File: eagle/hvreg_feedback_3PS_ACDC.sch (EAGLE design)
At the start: 17 parts

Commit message: capacitor bank
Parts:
- C5, C6: device rcl:C-US225-108X268 -> rcl:C-US275-205X316
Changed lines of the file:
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@@
 <grid distance="0.1" unitdist="inch" unit="inch" style="lines" multiple="1" display="no" altdistance="0.01" altunitdist="inch" altunit="inch"/>
 <layers>
-<layer number="1" name="Top" color="4" fill="1" visible="no" active="no"/>
-<layer number="2" name="Route2" color="1" fill="3" visible="no" active="no"/>
-<layer number="3" name="Route3" color="4" fill="3" visible="no" active="no"/>
-<layer number="4" name="Route4" color="1" fill="4" visible="no" active="no"/>
-<layer number="5" name="Route5" color="4" fill="4" visible="no" active="no"/>
-<layer number="6" name="Route6" color="1" fill="8" visible="no" active="no"/>
-<layer number="7" name="Route7" color="4" fill="8" visible="no" active="no"/>
-<layer number="8" name="Route8" color="1" fill="2" visible="no" active="no"/>
-<layer number="9" name="Route9" color="4" fill="2" visible="no" active="no"/>
-<layer number="10" name="Route10" color="1" fill="7" visible="no" active="no"/>
-<layer number="11" name="Route11" color="4" fill="7" visible="no" active="no"/>
-<layer number="12" name="Route12" color="1" fill="5" visible="no" active="no"/>
-<layer number="13" name="Route13" color="4" fill="5" visible="no" active="no"/>
-<layer number="14" name="Route14" color="1" fill="6" visible="no" active="no"/>
-<layer number="15" name="Route15" color="4" fill="6" visible="no" active="no"/>
-<layer number="16" name="Bottom" color="1" fill="1" visible="no" active="no"/>
-<layer number="17" name="Pads" color="2" fill="1" visible="no" active="no"/>
-<layer number="18" name="Vias" color="2" fill="1" visible="no" active="no"/>
-<layer number="19" name="Unrouted" color="6" fill="1" visible="no" active="no"/>
-<layer number="20" name="Dimension" color="15" fill="1" visible="no" active="no"/>
-<layer number="21" name="tPlace" color="7" fill="1" visible="no" active="no"/>
-<layer number="22" name="bPlace" color="7" fill="1" visible="no" active="no"/>
-<layer number="23" name="tOrigins" color="15" fill="1" visible="no" active="no"/>
-<layer number="24" name="bOrigins" color="15" fill="1" visible="no" active="no"/>
-<layer number="25" name="tNames" color="7" fill="1" visible="no" active="no"/>
-<layer number="26" name="bNames" color="7" fill="1" visible="no" active="no"/>
-<layer number="27" name="tValues" color="7" fill="1" visible="no" active="no"/>
-<layer number="28" name="bValues" color="7" fill="1" visible="no" active="no"/>
+<layer number="1" name="Top" color="4" fill="1" visible="yes" active="no"/>
+<layer number="2" name="Route2" color="1" fill="3" visible="yes" active="no"/>
+<layer number="3" name="Route3" color="4" fill="3" visible="yes" active="no"/>
+<layer number="4" name="Route4" color="1" fill="4" visible="yes" active="no"/>
+<layer number="5" name="Route5" color="4" fill="4" visible="yes" active="no"/>
+<layer number="6" name="Route6" color="1" fill="8" visible="yes" active="no"/>
+<layer number="7" name="Route7" color="4" fill="8" visible="yes" active="no"/>
+<layer number="8" name="Route8" color="1" fill="2" visible="yes" active="no"/>
+<layer number="9" name="Route9" color="4" fill="2" visible="yes" active="no"/>
+<layer number="10" name="Route10" color="1" fill="7" visible="yes" active="no"/>
+<layer number="11" name="Route11" color="4" fill="7" visible="yes" active="no"/>
+<layer number="12" name="Route12" color="1" fill="5" visible="yes" active="no"/>
+<layer number="13" name="Route13" color="4" fill="5" visible="yes" active="no"/>
+<layer number="14" name="Route14" color="1" fill="6" visible="yes" active="no"/>
+<layer number="15" name="Route15" color="4" fill="6" visible="yes" active="no"/>
+<layer number="16" name="Bottom" color="1" fill="1" visible="yes" active="no"/>
+<layer number="17" name="Pads" color="2" fill="1" visible="yes" active="no"/>
+<layer number="18" name="Vias" color="2" fill="1" visible="yes" active="no"/>
+<layer number="19" name="Unrouted" color="6" fill="1" visible="yes" active="no"/>
+<layer number="20" name="Dimension" color="15" fill="1" visible="yes" active="no"/>
+<layer number="21" name="tPlace" color="7" fill="1" visible="yes" active="no"/>
+<layer number="22" name="bPlace" color="7" fill="1" visible="yes" active="no"/>
+<layer number="23" name="tOrigins" color="15" fill="1" visible="yes" active="no"/>
+<layer number="24" name="bOrigins" color="15" fill="1" visible="yes" active="no"/>
+<layer number="25" name="tNames" color="7" fill="1" visible="yes" active="no"/>
+<layer number="26" name="bNames" color="7" fill="1" visible="yes" active="no"/>
+<layer number="27" name="tValues" color="7" fill="1" visible="yes" active="no"/>
+<layer number="28" name="bValues" color="7" fill="1" visible="yes" active="no"/>
 <layer number="29" name="tStop" color="7" fill="3" visible="no" active="no"/>
 <layer number="30" name="bStop" color="7" fill="6" visible="no" active="no"/>
@@
 <layer number="35" name="tGlue" color="7" fill="4" visible="no" active="no"/>
 <layer number="36" name="bGlue" color="7" fill="5" visible="no" active="no"/>
-<layer number="37" name="tTest" color="7" fill="1" visible="no" active="no"/>
-<layer number="38" name="bTest" color="7" fill="1" visible="no" active="no"/>
+<layer number="37" name="tTest" color="7" fill="1" visible="yes" active="no"/>
+<layer number="38" name="bTest" color="7" fill="1" visible="yes" active="no"/>
 <layer number="39" name="tKeepout" color="4" fill="11" visible="no" active="no"/>
 <layer number="40" name="bKeepout" color="1" fill="11" visible="no" active="no"/>
@@
 <layer number="44" name="Drills" color="7" fill="1" visible="no" active="no"/>
 <layer number="45" name="Holes" color="7" fill="1" visible="no" active="no"/>
-<layer number="46" name="Milling" color="3" fill="1" visible="no" active="no"/>
-<layer number="47" name="Measures" color="7" fill="1" visible="no" active="no"/>
-<layer number="48" name="Document" color="7" fill="1" visible="no" active="no"/>
-<layer number="49" name="Reference" color="7" fill="1" visible="no" active="no"/>
-<layer number="50" name="dxf" color="7" fill="1" visible="no" active="no"/>
-<layer number="51" name="tDocu" color="7" fill="1" visible="no" active="no"/>
-<layer number="52" name="bDocu" color="7" fill="1" visible="no" active="no"/>
-<layer number="53" name="tGND_GNDA" color="7" fill="9" visible="no" active="no"/>
-<layer number="54" name="bGND_GNDA" color="1" fill="9" visible="no" active="no"/>
-<layer number="56" name="wert" color="7" fill="1" visible="no" active="no"/>
+<layer number="46" name="Milling" color="3" fill="1" visible="yes" active="no"/>
+<layer number="47" name="Measures" color="7" fill="1" visible="yes" active="no"/>
+<layer number="48" name="Document" color="7" fill="1" visible="yes" active="no"/>
+<layer number="49" name="Reference" color="7" fill="1" visible="yes" active="no"/>
+<layer number="50" name="dxf" color="7" fill="1" visible="yes" active="no"/>
+<layer number="51" name="tDocu" color="7" fill="1" visible="yes" active="no"/>
+<layer number="52" name="bDocu" color="7" fill="1" visible="yes" active="no"/>
+<layer number="53" name="tGND_GNDA" color="7" fill="9" visible="yes" active="no"/>
+<layer number="54" name="bGND_GNDA" color="1" fill="9" visible="yes" active="no"/>
+<layer number="56" name="wert" color="7" fill="1" visible="yes" active="no"/>
 <layer number="90" name="Modules" color="5" fill="1" visible="yes" active="yes"/>
 <layer number="91" name="Nets" color="2" fill="1" visible="yes" active="yes"/>
@@
 <part name="R2" library="pot" deviceset="TRIM_US-" device="B90P"/>
 <part name="R3" library="pot" deviceset="TRIM_US-" device="B90P"/>
-<part name="C5" library="rcl" deviceset="C-US" device="225-108X268" value="1u"/>
-<part name="C6" library="rcl" deviceset="C-US" device="225-108X268" value="1u"/>
+<part name="C5" library="rcl" deviceset="C-US" device="275-205X316" value="1u"/>
+<part name="C6" library="rcl" deviceset="C-US" device="275-205X316" value="1u"/>
 <part name="GND16" library="supply1" deviceset="GND" device=""/>
 <part name="LV+" library="testpad" deviceset="TP" device="PAD1-20Y"/>

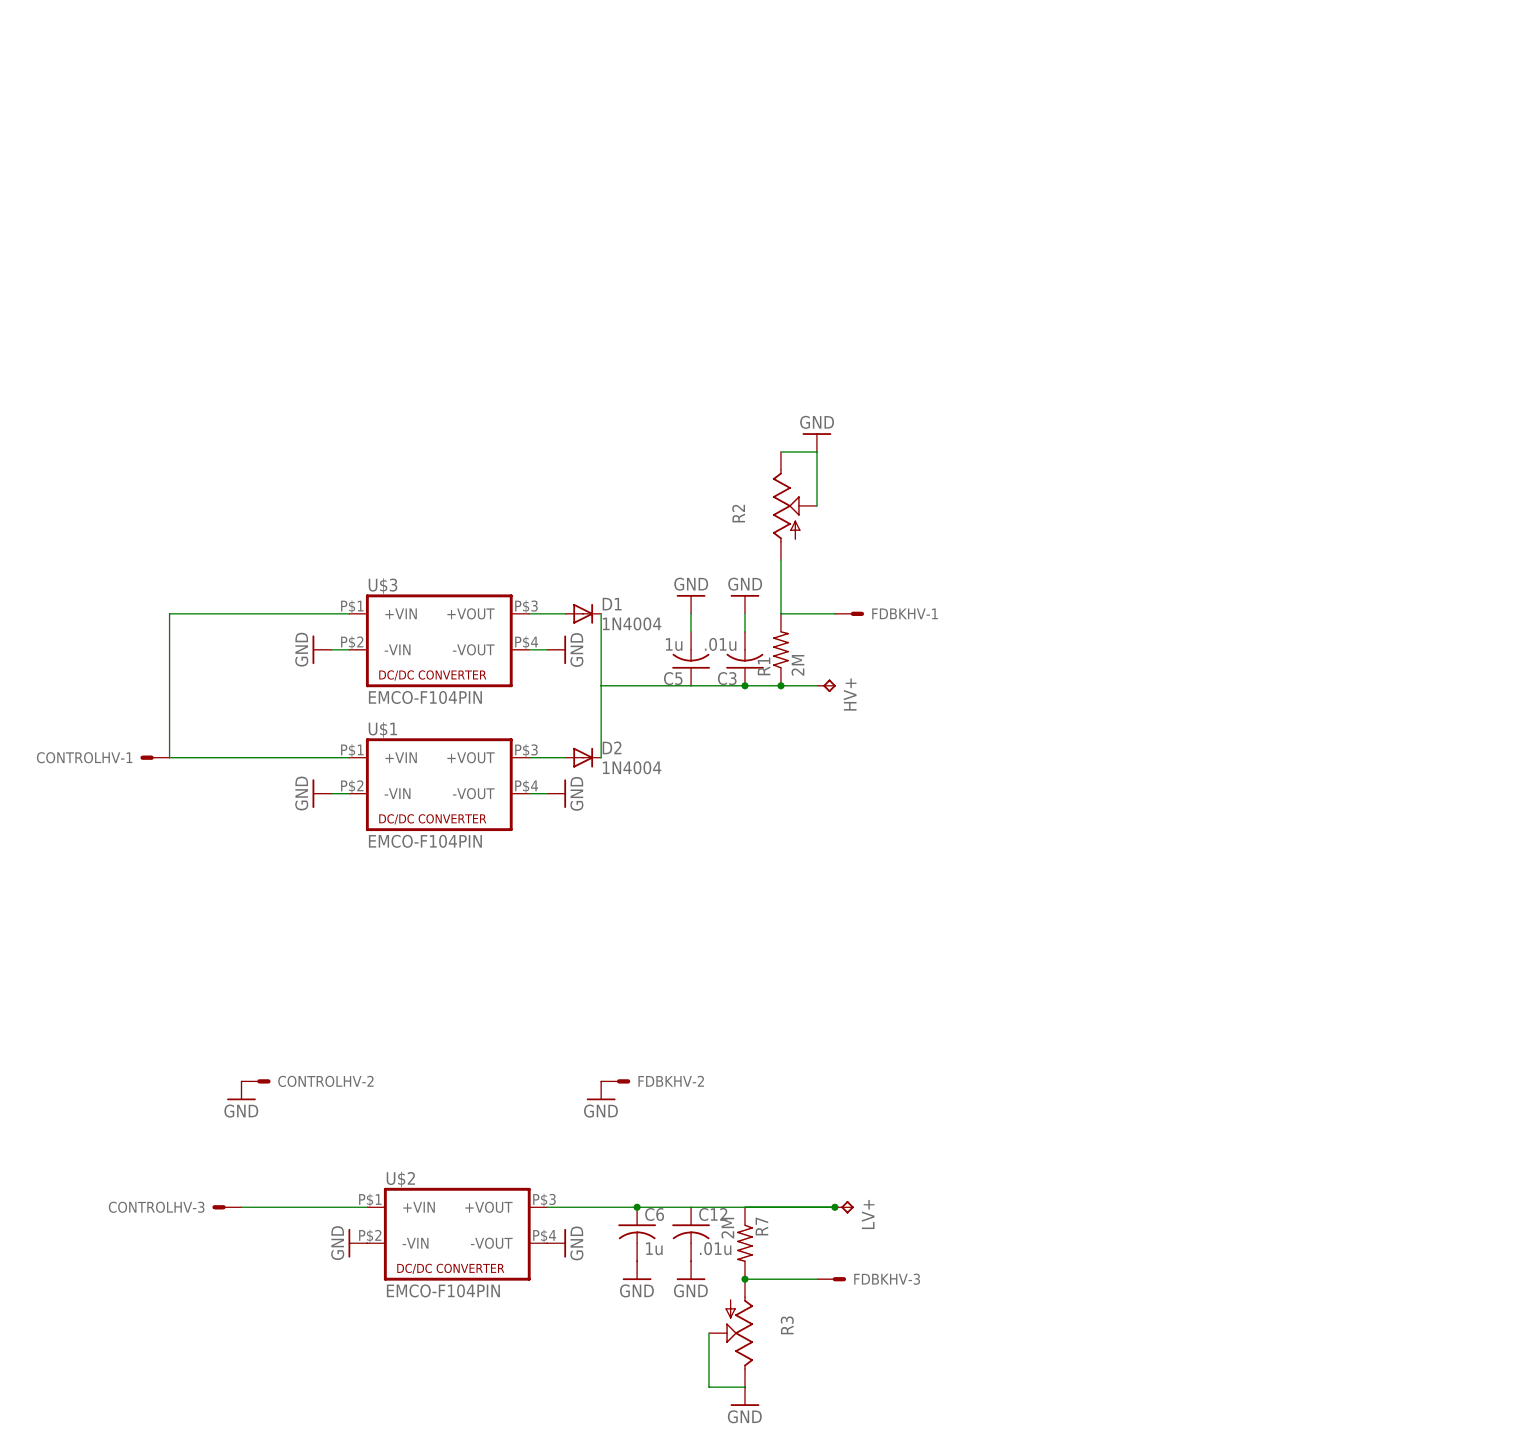
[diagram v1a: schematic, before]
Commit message: tweaks. still need bigger vias for zeners and hv resistors
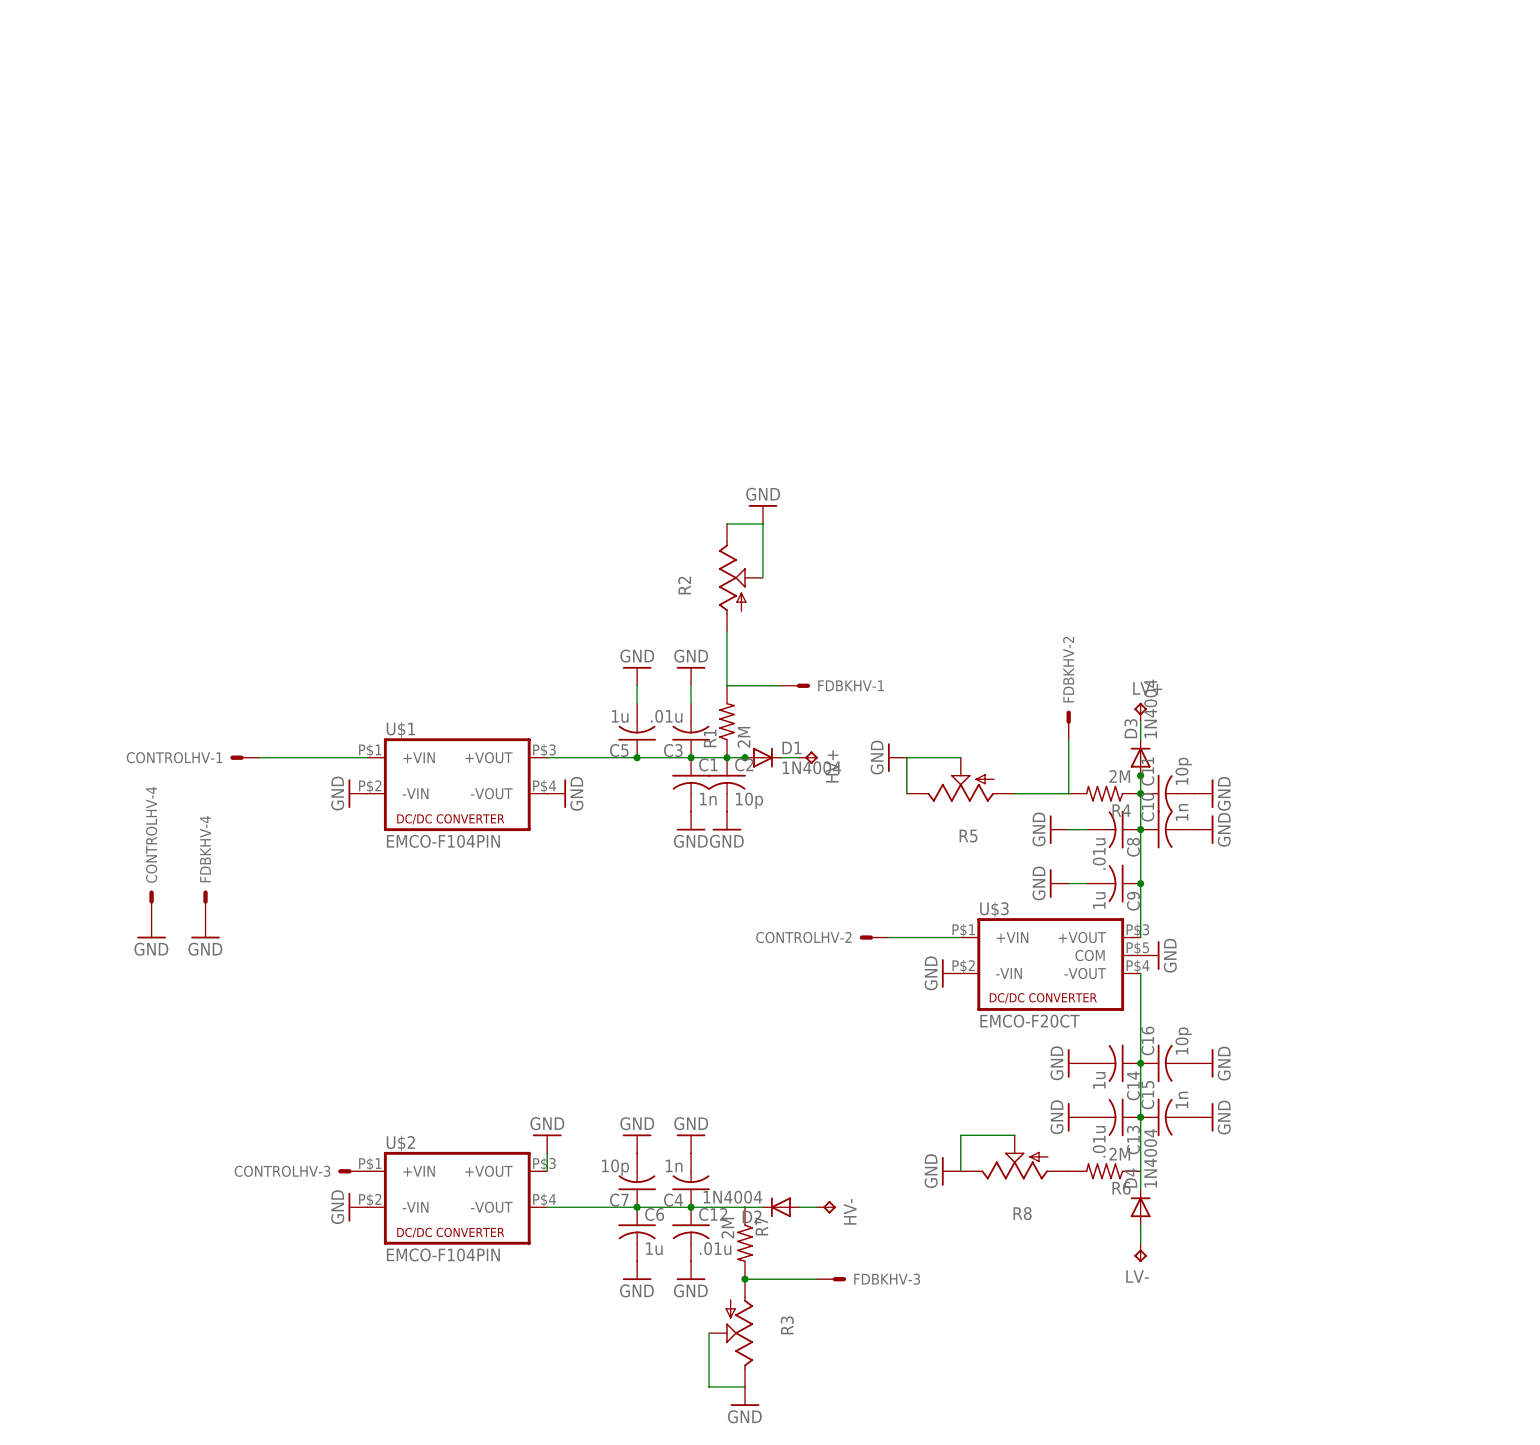
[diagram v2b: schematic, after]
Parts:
- added C1, C10, C15, C4: 1n, rcl:C-US075-042X103
- added C11, C16, C2, C7: 10p, rcl:C-US075-042X103
- added C13, C8: .01u, rcl:C-US075-042X103
- added C14, C9: 1u, rcl:C-US275-205X316
- added D3, D4: 1N4004, diode:1N4004
- added HV-, LV-: TPPAD1-20Y, testpad:TPPAD1-20Y
- added R4, R6: 2M, resistor:R-US_0207/12
- added R5, R8: (no value), pot:TRIM_US-B90P
- CONTROLHV, FDBKHV: device con-molex:KK-156-3 -> con-molex:KK-156-4
- U$3: value EMCO-F104PIN -> EMCO-F20CT; device dc-dc-converter:EMCO-F104PIN -> dc-dc-converter:EMCO-F20CT
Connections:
- new net N$1: C1.1, C2.1, C3.1, C5.1, D1.A, R1.1, U$1.+VOUT
- new net N$10: C13.1, C14.1, C15.1, C16.1, D4.C, R6.1
- new net N$11: R6.2, R8.A
- new net N$12: D4.A, LV-.TP
- new net N$13: CONTROLHV-1.S, U$1.+VIN
- new net N$14: CONTROLHV-2.S, U$3.+VIN
- new net N$5: C10.1, C11.1, C8.1, C9.1, D3.A, R4.1
- net GND: now also C1.2, C10.2, C11.2, C13.2, C14.2, C15.2, C16.2, C2.2, C4.2, C7.2, C8.2, C9.2, CONTROLHV-4.S, FDBKHV-4.S, R5.E, R5.S, R8.E, R8.S, U$2.+VOUT, U$3.COM; no longer CONTROLHV-2.S, FDBKHV-2.S, U$2.-VOUT, U$3.-VOUT
- net N$2: now also C4.1, C7.1, D2.C, U$2.-VOUT; no longer LV+.TP, U$2.+VOUT
- net N$4: now also D2.A, HV-.TP; no longer CONTROLHV-1.S, U$1.+VIN, U$3.+VIN
- net N$6: now also D1.C, HV+.TP; no longer D1.A, U$3.+VOUT
- net N$7: now also FDBKHV-2.S, R4.2, R5.A; no longer D2.A, U$1.+VOUT
- net N$9: now also D3.C, LV+.TP; no longer C3.1, C5.1, D1.C, D2.C, HV+.TP, R1.1
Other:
- moved on the sheet: C3, C5, CONTROLHV-1, CONTROLHV-2, CONTROLHV-3, D1, D2, FDBKHV-1, FDBKHV-2, HV+, LV+, R1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

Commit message: layout fixes
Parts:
- removed R6: 2M, resistor:R-US_0207/12
- removed R8: (no value), pot:TRIM_US-B90P
- C1, C2, C3: device rcl:C-US075-042X103 -> rcl:C-US102-043X133
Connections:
- removed net N$11: R6.2, R8.A
- net GND: no longer R8.E, R8.S
- net N$10: no longer R6.1

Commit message: smd
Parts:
- C10, C11, C12, C13, C15, C16, C4, C7, C8: device rcl:C-US075-042X103 -> rcl:C-US102-043X133
- R1, R4, R7: device resistor:R-US_0207/12 -> resistor:R-US_0613/15
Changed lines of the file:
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@@
 <part name="GND9" library="supply1" deviceset="GND" device=""/>
 <part name="GND17" library="supply1" deviceset="GND" device=""/>
-<part name="C12" library="rcl" deviceset="C-US" device="075-042X103" value=".01u"/>
-<part name="R1" library="resistor" deviceset="R-US_" device="0207/12" value="2M"/>
-<part name="R7" library="resistor" deviceset="R-US_" device="0207/12" value="2M"/>
+<part name="C12" library="rcl" deviceset="C-US" device="102-043X133" value=".01u"/>
+<part name="R1" library="resistor" deviceset="R-US_" device="0613/15" value="2M"/>
+<part name="R7" library="resistor" deviceset="R-US_" device="0613/15" value="2M"/>
 <part name="GND5" library="supply1" deviceset="GND" device=""/>
 <part name="GND12" library="supply1" deviceset="GND" device=""/>
@@
 <part name="GND8" library="supply1" deviceset="GND" device=""/>
 <part name="GND10" library="supply1" deviceset="GND" device=""/>
-<part name="C4" library="rcl" deviceset="C-US" device="075-042X103" value="1n"/>
-<part name="C7" library="rcl" deviceset="C-US" device="075-042X103" value="10p"/>
+<part name="C4" library="rcl" deviceset="C-US" device="102-043X133" value="1n"/>
+<part name="C7" library="rcl" deviceset="C-US" device="102-043X133" value="10p"/>
 <part name="GND11" library="supply1" deviceset="GND" device=""/>
 <part name="GND13" library="supply1" deviceset="GND" device=""/>
@@
 <part name="GND14" library="supply1" deviceset="GND" device=""/>
 <part name="LV+" library="testpad" deviceset="TP" device="PAD1-20Y"/>
-<part name="C8" library="rcl" deviceset="C-US" device="075-042X103" value=".01u"/>
+<part name="C8" library="rcl" deviceset="C-US" device="102-043X133" value=".01u"/>
 <part name="GND18" library="supply1" deviceset="GND" device=""/>
-<part name="R4" library="resistor" deviceset="R-US_" device="0207/12" value="2M"/>
+<part name="R4" library="resistor" deviceset="R-US_" device="0613/15" value="2M"/>
 <part name="GND19" library="supply1" deviceset="GND" device=""/>
 <part name="R5" library="pot" deviceset="TRIM_US-" device="B90P"/>
 <part name="C9" library="rcl" deviceset="C-US" device="275-205X316" value="1u"/>
 <part name="GND20" library="supply1" deviceset="GND" device=""/>
-<part name="C10" library="rcl" deviceset="C-US" device="075-042X103" value="1n"/>
-<part name="C11" library="rcl" deviceset="C-US" device="075-042X103" value="10p"/>
+<part name="C10" library="rcl" deviceset="C-US" device="102-043X133" value="1n"/>
+<part name="C11" library="rcl" deviceset="C-US" device="102-043X133" value="10p"/>
 <part name="GND21" library="supply1" deviceset="GND" device=""/>
 <part name="GND22" library="supply1" deviceset="GND" device=""/>
 <part name="D3" library="diode" deviceset="1N4004" device=""/>
 <part name="GND23" library="supply1" deviceset="GND" device=""/>
-<part name="C13" library="rcl" deviceset="C-US" device="075-042X103" value=".01u"/>
+<part name="C13" library="rcl" deviceset="C-US" device="102-043X133" value=".01u"/>
 <part name="C14" library="rcl" deviceset="C-US" device="275-205X316" value="1u"/>
 <part name="GND25" library="supply1" deviceset="GND" device=""/>
 <part name="LV-" library="testpad" deviceset="TP" device="PAD1-20Y"/>
-<part name="C15" library="rcl" deviceset="C-US" device="075-042X103" value="1n"/>
-<part name="C16" library="rcl" deviceset="C-US" device="075-042X103" value="10p"/>
+<part name="C15" library="rcl" deviceset="C-US" device="102-043X133" value="1n"/>
+<part name="C16" library="rcl" deviceset="C-US" device="102-043X133" value="10p"/>
 <part name="GND26" library="supply1" deviceset="GND" device=""/>
 <part name="GND27" library="supply1" deviceset="GND" device=""/>
